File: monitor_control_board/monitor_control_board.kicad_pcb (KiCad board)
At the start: 2 copper layers, 50 x 58 mm, 21 parts, among them J1 Conn_01x09_Male, J2 Conn_01x09_Male, J3 Conn_01x05_Male, J4 Conn_01x05_Male, SW1 SW_Push, SW2 SW_Push, SW3 SW_Push, SW4 SW_Push, SW5 SW_Push, SW6 SW_Push, U1 TSSP58038

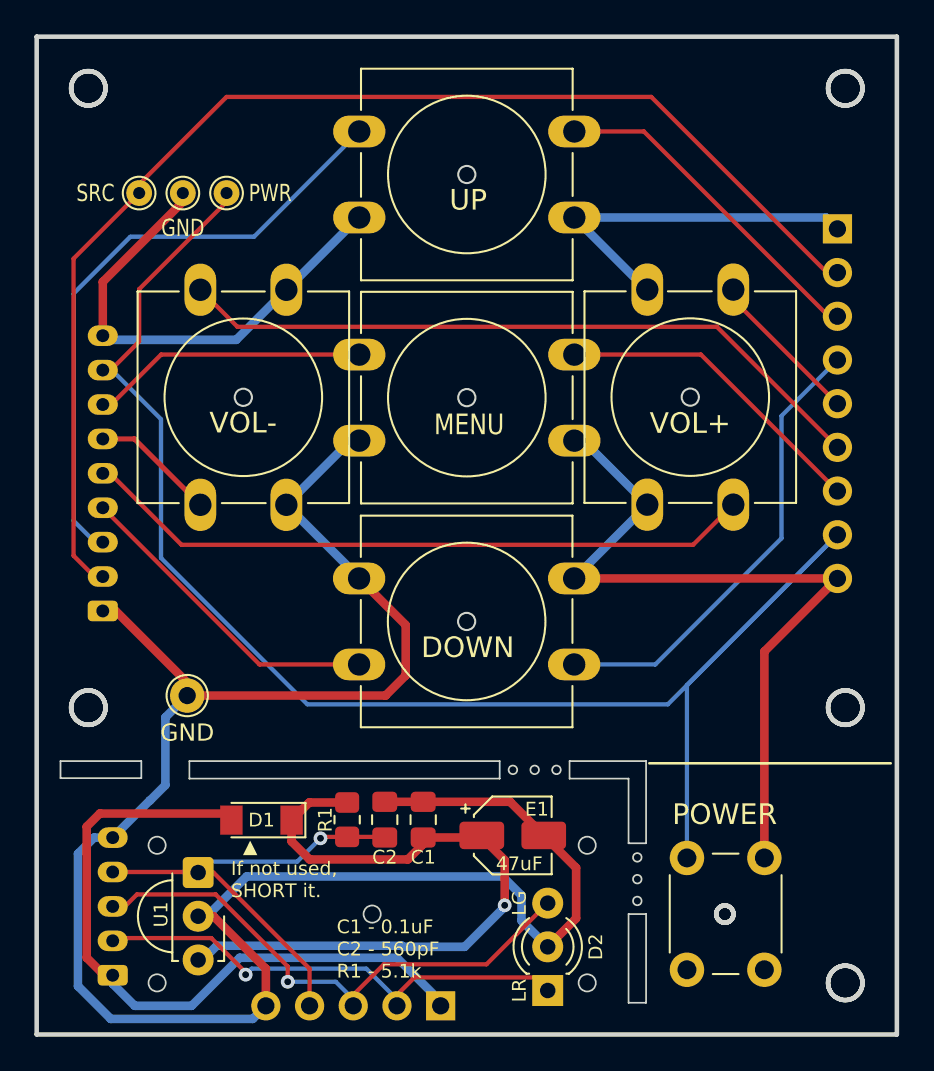
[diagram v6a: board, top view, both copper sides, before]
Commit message: monitor_osd 커넥터 모양 및 위치 변경
Signed-off-by: Ju, Gyeong-min <jcmh74@gmail.com>
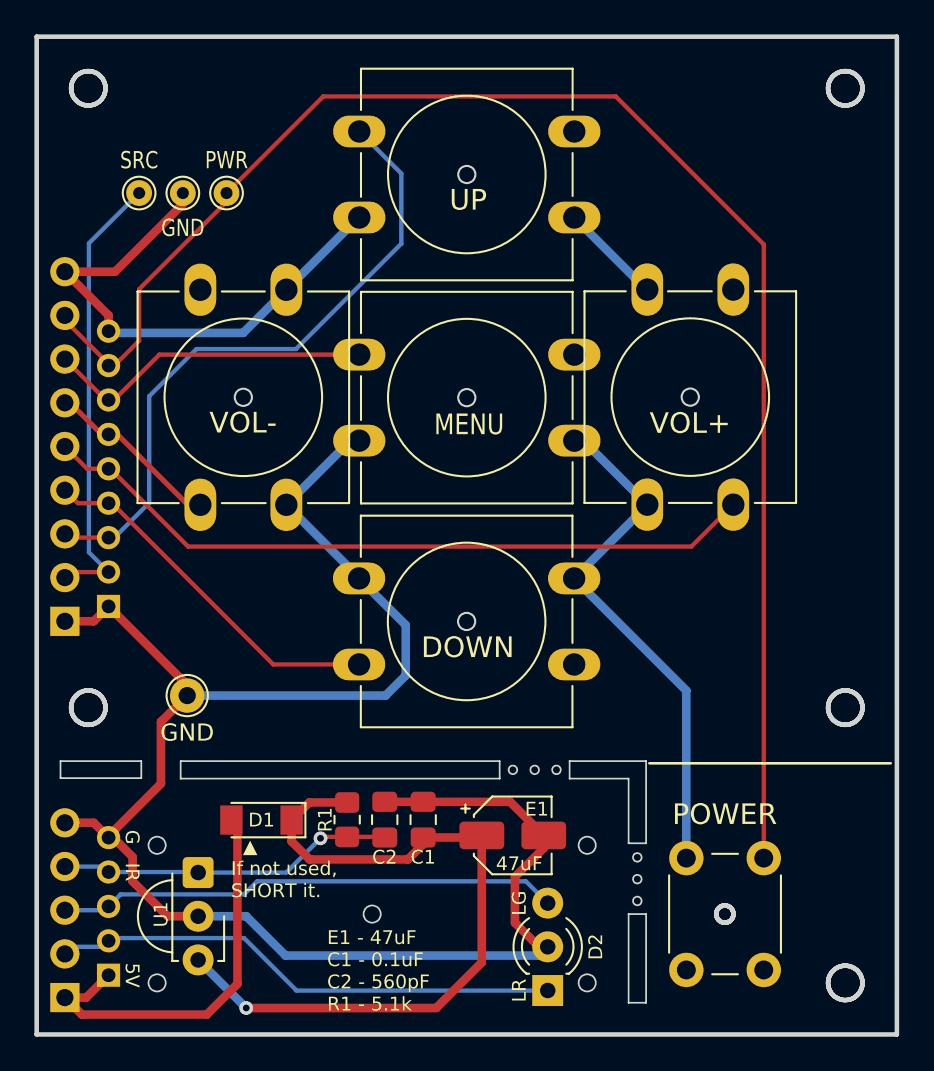
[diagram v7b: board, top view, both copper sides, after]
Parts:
- J1: value Conn_01x09_Male -> Conn_01x09; footprint Connector_JST:JST_PH_S9B-PH-K_1x09_P2.00mm_Horizontal -> Connector_PinHeader_2.00mm:PinHeader_1x09_P2.00mm_Vertical
- J2: value Conn_01x09_Male -> Conn_01x09
- J3: value Conn_01x05_Male -> Conn_01x05; footprint Connector_JST:JST_PH_S5B-PH-K_1x05_P2.00mm_Horizontal -> Connector_PinHeader_2.00mm:PinHeader_1x05_P2.00mm_Vertical
- J4: value Conn_01x05_Male -> Conn_01x05
- moved J2 50.4 mm to (130.3, 95.8), turned to 0 degrees
- moved J4 21.8 mm to (130.3, 117.6), turned to 0 degrees
- moved SW6 7.88 mm to (170.9, 109.5), turned to -90 degrees
- moved J1 0.43 mm to (132.8, 94.9), turned to 0 degrees
- moved J3 0.24 mm to (132.8, 116.3), turned to 0 degrees
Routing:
- net /SOURCE: track 72.3 -> 26.4 mm
- net GND: track 215.4 -> 170.3 mm
- net /VOL_M: track 48.1 -> 10.3 mm
- net /DOWN: track 45.5 -> 21.3 mm
- net /UP: track 55.7 -> 37.9 mm
- net +5V: track 41.0 -> 23.9 mm
- net /MENU: track 34.7 -> 19.2 mm
- net /IRIN: track 27.7 -> 19.3 mm
- net /VOL_P: track 48.5 -> 42.3 mm
- net /POWER: track 95.5 -> 89.8 mm
- net /LED_G: track 31.8 -> 29.3 mm, vias 1 -> 0
- net Net-(C1-Pad1): track 41.0 -> 43.3 mm
- net /LED_R: track 28.9 -> 29.7 mm, vias 1 -> 0
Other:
- outline, holes or cut-outs redrawn
- board text added: "E1 - 47uF C1 - 0.1uF C2 - 560pF R1 - 5.1k"
- board text removed: "C1 - 0.1uF C2 - 560pF R1 - 5.1k"
- board text removed: "Conn_01x08_Male"
